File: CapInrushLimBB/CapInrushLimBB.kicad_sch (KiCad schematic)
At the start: 27 parts, among them J1 Screw_Terminal_01x02, J2 Screw_Terminal_01x02, K1 G5LE-1A, Q1 MPSA42, Q2 IRF9540N, Q3 MPSA42, Q4 Q_PMOS_GDSD

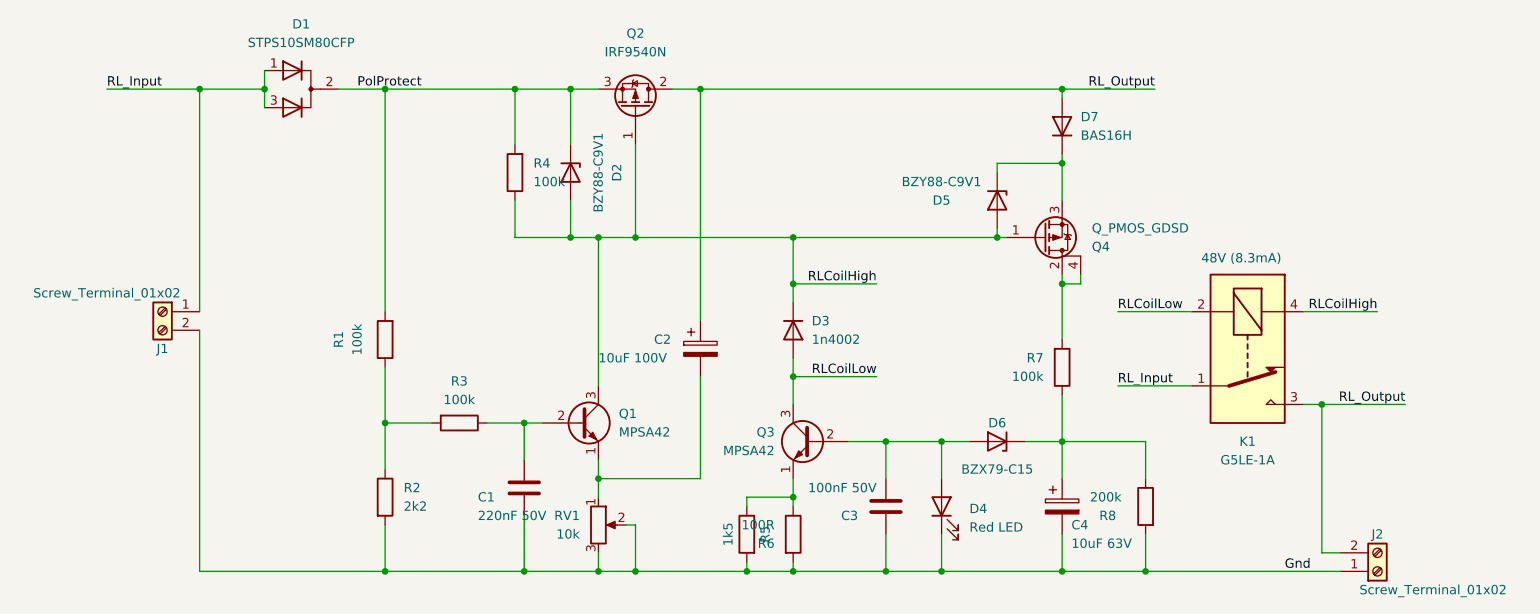
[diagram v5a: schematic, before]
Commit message: Tweaked BJT footprint (custom) to increase clearance and tweaked track positions accordingly.
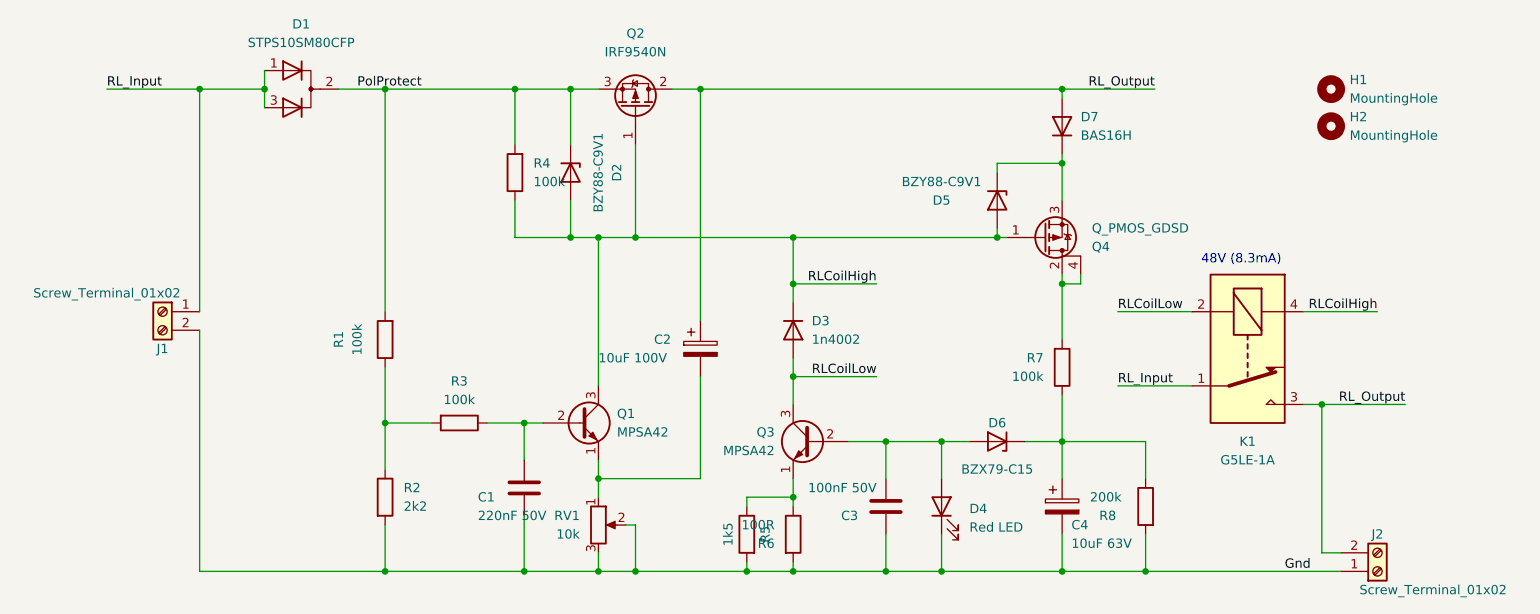
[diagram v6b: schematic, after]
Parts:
- added H1, H2: MountingHole, MountingHole:MountingHole_3.2mm_M3, symbol Mechanical:MountingHole
- Q1, Q3: footprint Package_TO_SOT_THT:TO-92_Inline -> CapInrushLim:TO-92_Inline
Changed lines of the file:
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@@
     (pin "2")
+  )
+  (symbol (lib_id "Mechanical:MountingHole") (at 198.12 73.66 0) (unit 1)
+    (in_bom yes) (on_board yes) (fields_autoplaced)
+    (property "Reference" "H1" (id 0) (at 200.66 72.3899 0)
+      (effects (font (size 1.27 1.27)) (justify left))
+    )
+    (property "Value" "MountingHole" (id 1) (at 200.66 74.9299 0)
+      (effects (font (size 1.27 1.27)) (justify left))
+    )
+    (property "Footprint" "MountingHole:MountingHole_3.2mm_M3" (id 2) (at 198.12 73.66 0)
+      (effects (font (size 1.27 1.27)) hide)
+    )
+    (property "Datasheet" "~" (id 3) (at 198.12 73.66 0)
+      (effects (font (size 1.27 1.27)) hide)
+    )
   )
   (symbol (lib_id "Device:D") (at 161.29 78.74 90) (unit 1)
@@
     (pin "4")
   )
+  (symbol (lib_id "Mechanical:MountingHole") (at 198.12 78.74 0) (unit 1)
+    (in_bom yes) (on_board yes) (fields_autoplaced)
+    (property "Reference" "H2" (id 0) (at 200.66 77.4699 0)
+      (effects (font (size 1.27 1.27)) (justify left))
+    )
+    (property "Value" "MountingHole" (id 1) (at 200.66 80.0099 0)
+      (effects (font (size 1.27 1.27)) (justify left))
+    )
+    (property "Footprint" "MountingHole:MountingHole_3.2mm_M3" (id 2) (at 198.12 78.74 0)
+      (effects (font (size 1.27 1.27)) hide)
+    )
+    (property "Datasheet" "~" (id 3) (at 198.12 78.74 0)
+      (effects (font (size 1.27 1.27)) hide)
+    )
+  )
   (symbol (lib_id "Device:D_Zener") (at 152.4 121.92 180) (unit 1)
     (in_bom yes) (on_board yes)
@@
       (effects (font (size 1.27 1.27)) (justify left))
     )
-    (property "Footprint" "Package_TO_SOT_THT:TO-92_Inline" (id 2) (at 121.92 123.825 0)
+    (property "Footprint" "CapInrushLim:TO-92_Inline" (id 2) (at 121.92 123.825 0)
       (effects (font (size 1.27 1.27) italic) (justify left) hide)
     )
@@
   (symbol (lib_id "Transistor_BJT:MPSA42") (at 95.25 119.38 0) (unit 1)
     (in_bom yes) (on_board yes) (fields_autoplaced)
-    (property "Reference" "Q1" (id 0) (at 100.584 118.1099 0)
-      (effects (font (size 1.27 1.27)) (justify left))
-    )
-    (property "Value" "MPSA42" (id 1) (at 100.584 120.6499 0)
-      (effects (font (size 1.27 1.27)) (justify left))
-    )
-    (property "Footprint" "Package_TO_SOT_THT:TO-92_Inline" (id 2) (at 100.33 121.285 0)
+    (property "Reference" "Q1" (id 0) (at 100.33 118.1099 0)
+      (effects (font (size 1.27 1.27)) (justify left))
+    )
+    (property "Value" "MPSA42" (id 1) (at 100.33 120.6499 0)
+      (effects (font (size 1.27 1.27)) (justify left))
+    )
+    (property "Footprint" "CapInrushLim:TO-92_Inline" (id 2) (at 100.33 121.285 0)
       (effects (font (size 1.27 1.27) italic) (justify left) hide)
     )
@@
       (reference "D7") (unit 1) (value "BAS16H") (footprint "Diode_SMD:D_SOD-323_HandSoldering")
     )
+    (path "/45090962-2083-441b-9cfd-a97a7818b434"
+      (reference "H1") (unit 1) (value "MountingHole") (footprint "MountingHole:MountingHole_3.2mm_M3")
+    )
+    (path "/8a39d130-9a9e-47ab-892a-be521946a0c9"
+      (reference "H2") (unit 1) (value "MountingHole") (footprint "MountingHole:MountingHole_3.2mm_M3")
+    )
     (path "/670b39a3-baf9-475d-9b0c-feda51bc6306"
       (reference "J1") (unit 1) (value "Screw_Terminal_01x02") (footprint "TerminalBlock:TerminalBlock_Altech_AK300-2_P5.00mm")
@@
     )
     (path "/a9f6f942-45df-4f12-8f1d-f9e51724c8de"
-      (reference "Q1") (unit 1) (value "MPSA42") (footprint "Package_TO_SOT_THT:TO-92_Inline")
+      (reference "Q1") (unit 1) (value "MPSA42") (footprint "CapInrushLim:TO-92_Inline")
     )
     (path "/2212c386-7c5c-4c1f-bd84-6a0d9986cbcc"
@@
     )
     (path "/a87e54c8-8fc6-42fe-b94e-72d1ec7ebea5"
-      (reference "Q3") (unit 1) (value "MPSA42") (footprint "Package_TO_SOT_THT:TO-92_Inline")
+      (reference "Q3") (unit 1) (value "MPSA42") (footprint "CapInrushLim:TO-92_Inline")
     )
     (path "/73df3bcd-2a9d-48ad-b04a-af9ee62e7631"

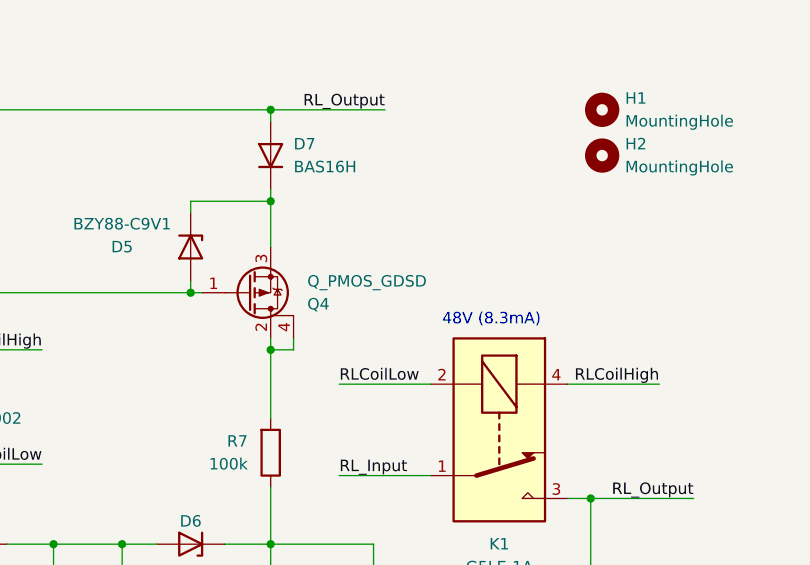
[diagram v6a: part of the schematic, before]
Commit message: Updated component value.
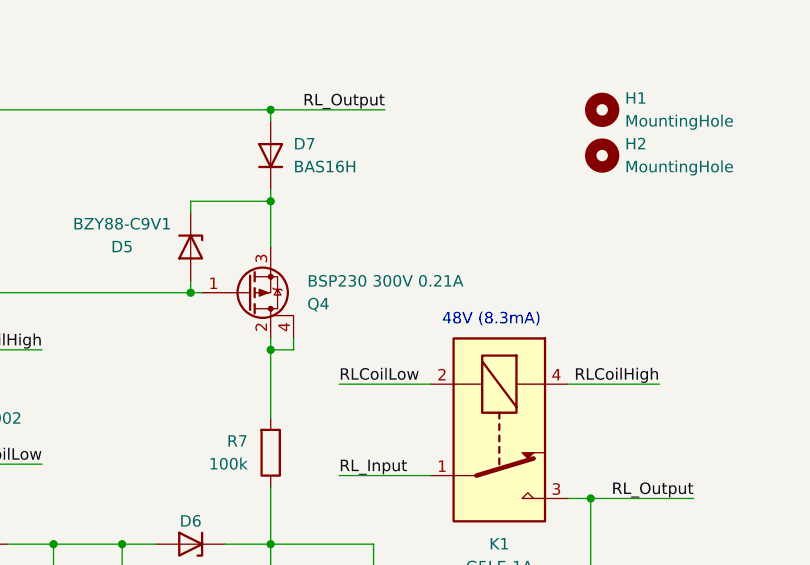
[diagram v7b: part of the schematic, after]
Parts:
- Q4: value Q_PMOS_GDSD -> BSP230 300V 0.21A
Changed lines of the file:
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@@
       (effects (font (size 1.27 1.27)) (justify left))
     )
-    (property "Value" "Q_PMOS_GDSD" (id 1) (at 165.354 92.7101 0)
+    (property "Value" "BSP230 300V 0.21A" (id 1) (at 165.354 92.7101 0)
       (effects (font (size 1.27 1.27)) (justify left))
     )
@@
     )
     (path "/73df3bcd-2a9d-48ad-b04a-af9ee62e7631"
-      (reference "Q4") (unit 1) (value "Q_PMOS_GDSD") (footprint "Package_TO_SOT_SMD:SOT-223")
+      (reference "Q4") (unit 1) (value "BSP230 300V 0.21A") (footprint "Package_TO_SOT_SMD:SOT-223")
     )
     (path "/1aaccc8b-a1cb-454a-b9d3-615d5ab3916e"

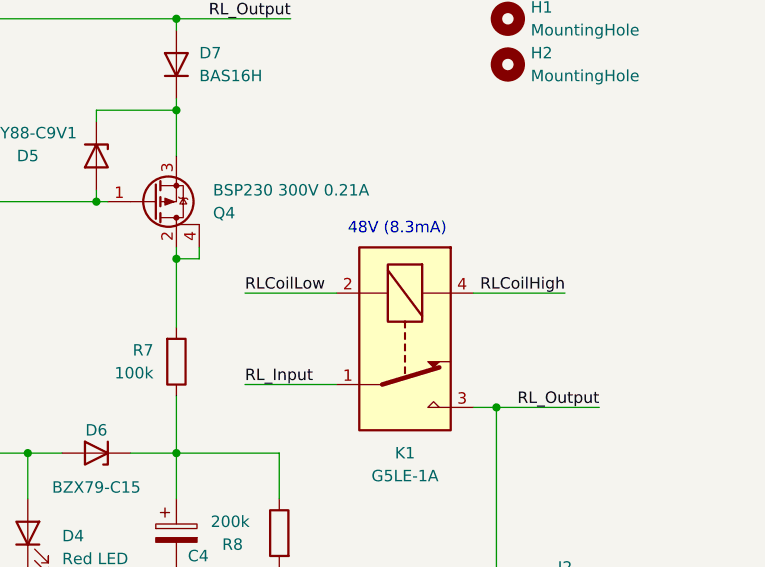
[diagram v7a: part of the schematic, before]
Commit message: Slight track tweak following assembly.
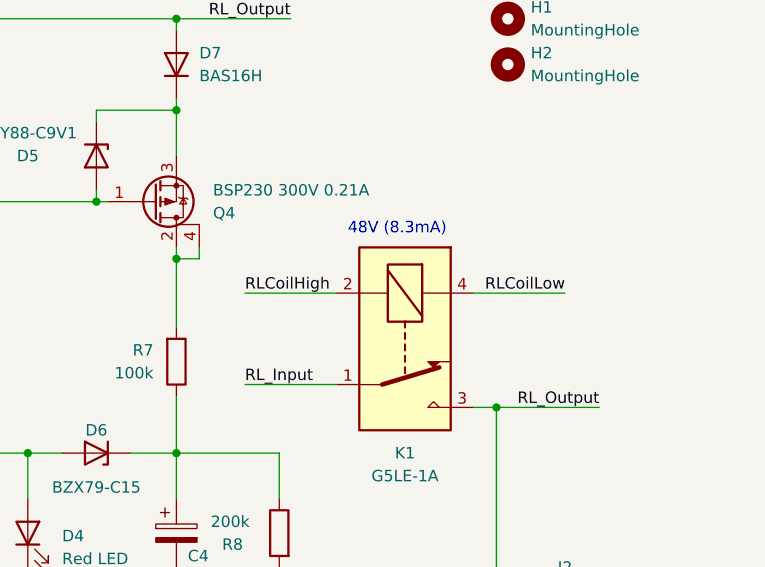
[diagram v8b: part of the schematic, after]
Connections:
- net RLCoilHigh: now also K1.2; no longer K1.4
- net RLCoilLow: now also K1.4; no longer K1.2
